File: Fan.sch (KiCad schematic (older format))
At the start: 9 parts, among them Q2 MOSFET_N, Q3 MOSFET_N, Q4 MOSFET_N, U4 OPA4170, U6 MCP4922-E/P

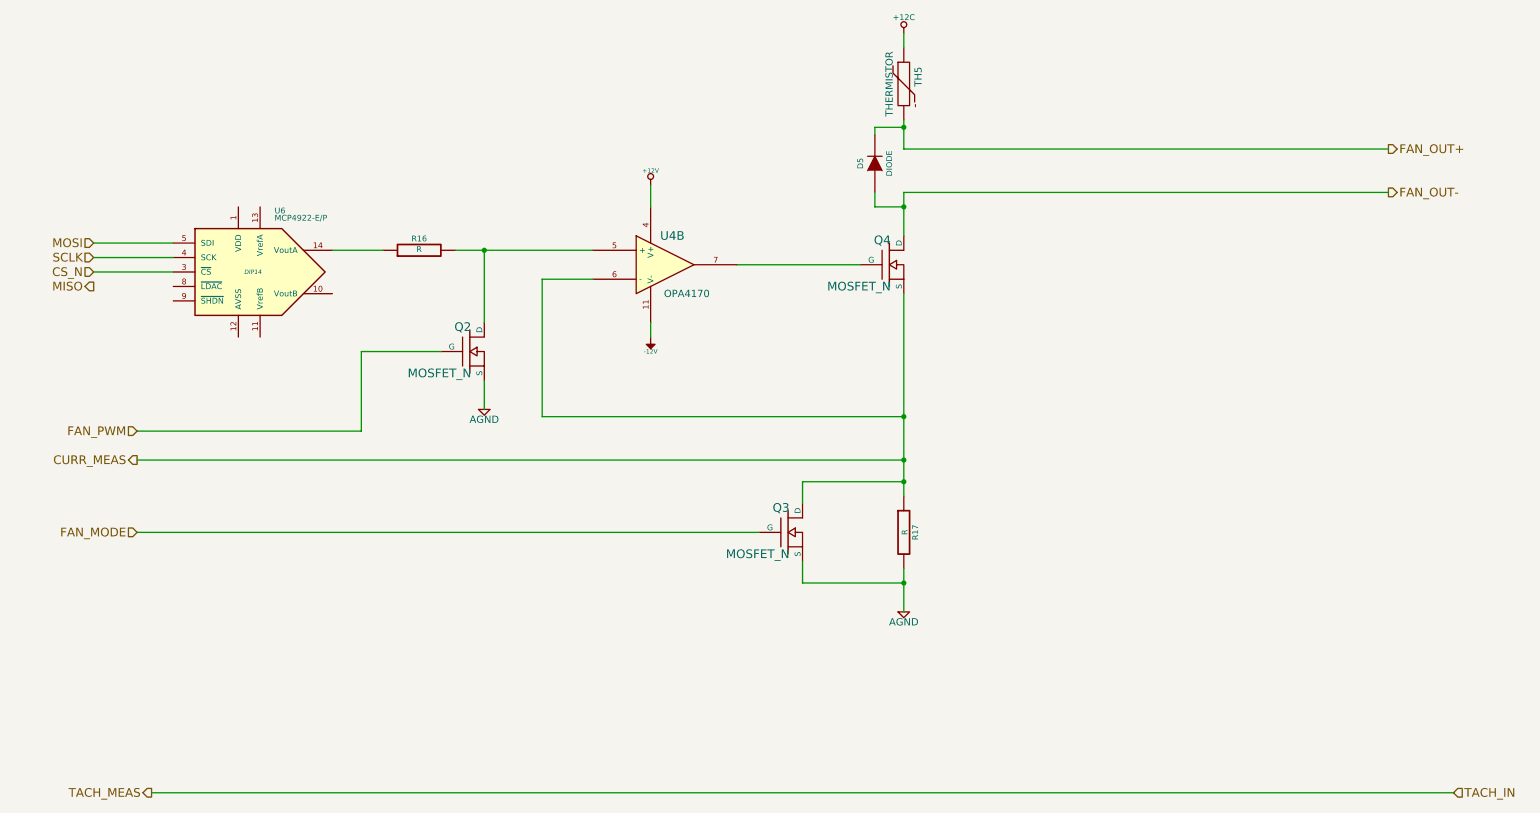
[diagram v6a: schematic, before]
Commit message: Fan driver: assc/placement
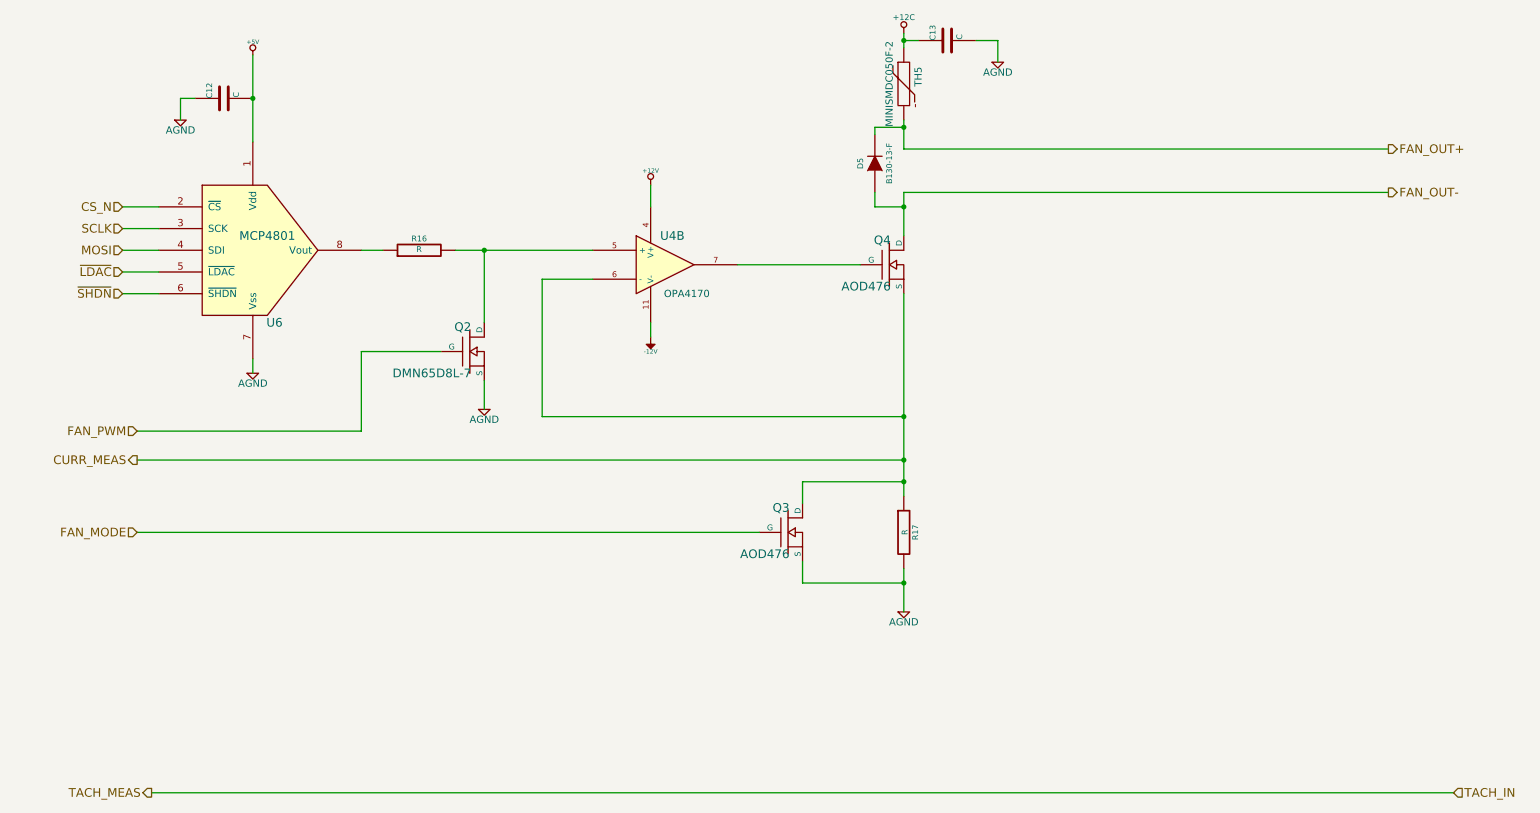
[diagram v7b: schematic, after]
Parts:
- removed Q3, Q4: MOSFET_N, ~, symbol MOSFET_N
- removed U6: MCP4922-E/P, DIP14, symbol MCP4922-E/P
- added C12, C13: C, ~, symbol C
- added Q3, Q4: AOD476, ~, symbol MOS_N_NUM
- added U6: MCP4801, symbol MCP4801
- D5: value DIODE -> B130-13-F; MFG Name (none) -> Diodes Inc; MFG Part Number (none) -> B130-13-F
- Q2: value MOSFET_N -> DMN65D8L-7; MFG Name (none) -> Diodes Inc; MFG Part Number (none) -> DMN65D8L-7
- TH5: value THERMISTOR -> MINISMDC050F-2; MFG Name (none) -> TE Connectivity; MFG Part Number (none) -> MINISMDC050F-2
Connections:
- net +12C: now also C13.1
- net AGND: now also C12.1, C13.2, Q3.3 (S), U6.7 (Vss)
- net CS_N: now also U6.2 (~CS)
- net CURR_MEAS: now also Q3.2 (D), Q4.3 (S)
- net FAN_MODE: now also Q3.1 (G)
- net FAN_OUT-: now also Q4.2 (D)
- net MOSI: now also U6.4 (SDI)
- net SCLK: now also U6.3 (SCK)
- net at U4.7: now also Q4.1 (G)
- net at R16.1: now also U6.8 (Vout)
- new net +5V: C12.2, U6.1 (Vdd)
- new net ~LDAC: U6.5 (~LDAC)
- new net ~SHDN: U6.6 (~SHDN)
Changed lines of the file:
@@
 $Descr A4 11693 8268
 encoding utf-8
-Sheet 5 9
+Sheet 4 9
 Title ""
-Date "22 feb 2014"
+Date "23 feb 2014"
 Rev ""
 Comp ""
@@
 $EndComp
 $Comp
-L MOSFET_N Q4
-U 1 1 52F44471
-P 6500 2500
-F 0 "Q4" H 6510 2670 60  0000 R CNN
-F 1 "MOSFET_N" H 6510 2350 60  0000 R CNN
-F 2 "~" H 6500 2500 60  0000 C CNN
-F 3 "~" H 6500 2500 60  0000 C CNN
-	1    6500 2500
-	1    0    0    -1
-$EndComp
-$Comp
 L R R17
 U 1 1 52F444AC
@@
 $EndComp
 $Comp
-L AGND #PWR25
+L AGND #PWR019
 U 1 1 52F444C1
 P 6600 4900
-F 0 "#PWR25" H 6600 4900 40  0001 C CNN
+F 0 "#PWR019" H 6600 4900 40  0001 C CNN
 F 1 "AGND" H 6600 4830 50  0000 C CNN
 F 2 "" H 6600 4900 60  0000 C CNN
@@
 $EndComp
 $Comp
-L +12V #PWR22
+L +12V #PWR020
 U 1 1 52F444E6
 P 4850 1950
-F 0 "#PWR22" H 4850 1900 20  0001 C CNN
+F 0 "#PWR020" H 4850 1900 20  0001 C CNN
 F 1 "+12V" H 4850 2050 30  0000 C CNN
 F 2 "" H 4850 1950 60  0000 C CNN
@@
 $EndComp
 $Comp
-L -12V #PWR23
+L -12V #PWR021
 U 1 1 52F444F9
 P 4850 3000
-F 0 "#PWR23" H 4850 3130 20  0001 C CNN
+F 0 "#PWR021" H 4850 3130 20  0001 C CNN
 F 1 "-12V" H 4850 3100 30  0000 C CNN
 F 2 "" H 4850 3000 60  0000 C CNN
@@
 $EndComp
 $Comp
-L AGND #PWR21
+L AGND #PWR022
 U 1 1 52F44588
 P 3700 3500
-F 0 "#PWR21" H 3700 3500 40  0001 C CNN
+F 0 "#PWR022" H 3700 3500 40  0001 C CNN
 F 1 "AGND" H 3700 3430 50  0000 C CNN
 F 2 "" H 3700 3500 60  0000 C CNN
@@
 	1    0    0    -1
 $EndComp
-$Comp
-L MCP4922-E/P U6
-U 1 1 52F445A1
-P 2100 2550
-F 0 "U6" H 2250 2950 40  0000 L BNN
-F 1 "MCP4922-E/P" H 2250 2900 40  0000 L BNN
-F 2 "DIP14" H 2100 2550 30  0000 C CIN
-F 3 "" H 2100 2550 60  0000 C CNN
-	1    2100 2550
-	1    0    0    -1
-$EndComp
 Text HLabel 1300 3850 0    60   Output ~ 0
 CURR_MEAS
-Text HLabel 1000 2350 0    60   Input ~ 0
+Text HLabel 1200 2400 0    60   Input ~ 0
 MOSI
-Text HLabel 1000 2650 0    60   Output ~ 0
-MISO
-Text HLabel 1000 2550 0    60   Input ~ 0
+Text HLabel 1200 2100 0    60   Input ~ 0
 CS_N
-Text HLabel 1000 2450 0    60   Input ~ 0
+Text HLabel 1200 2250 0    60   Input ~ 0
 SCLK
 Wire Wire Line
@@
 	1300 3850 6600 3850
 Connection ~ 6600 3850
-Wire Wire Line
-	1000 2350 1550 2350
-Wire Wire Line
-	1000 2450 1550 2450
-Wire Wire Line
-	1000 2550 1550 2550
 $Comp
 L R R16
@@
 	0    -1   -1   0
 $EndComp
-Wire Wire Line
-	3000 2400 2650 2400
-$Comp
-L MOSFET_N Q3
-U 1 1 52F7C941
-P 5800 4350
-F 0 "Q3" H 5810 4520 60  0000 R CNN
-F 1 "MOSFET_N" H 5810 4200 60  0000 R CNN
-F 2 "~" H 5800 4350 60  0000 C CNN
-F 3 "~" H 5800 4350 60  0000 C CNN
-	1    5800 4350
-	1    0    0    -1
-$EndComp
 $Comp
 L THERMISTOR TH5
@@
 P 6600 1250
 F 0 "TH5" V 6700 1300 50  0000 C CNN
-F 1 "THERMISTOR" V 6500 1250 50  0000 C CNN
+F 1 "MINISMDC050F-2" V 6500 1250 50  0000 C CNN
 F 2 "~" H 6600 1250 60  0000 C CNN
 F 3 "~" H 6600 1250 60  0000 C CNN
+F 4 "TE Connectivity" H 6600 1250 60  0001 C CNN "MFG Name"
+F 5 "MINISMDC050F-2" H 6600 1250 60  0001 C CNN "MFG Part Number"
 	1    6600 1250
 	1    0    0    -1
@@
 P 6400 1800
 F 0 "D5" H 6400 1900 40  0000 C CNN
-F 1 "DIODE" H 6400 1700 40  0000 C CNN
+F 1 "B130-13-F" H 6400 1700 40  0000 C CNN
 F 2 "~" H 6400 1800 60  0000 C CNN
 F 3 "~" H 6400 1800 60  0000 C CNN
+F 4 "Diodes Inc" H 6400 1800 60  0001 C CNN "MFG Name"
+F 5 "B130-13-F" H 6400 1800 60  0001 C CNN "MFG Part Number"
 	1    6400 1800
 	0    -1   -1   0
@@
 P 3600 3100
 F 0 "Q2" H 3610 3270 60  0000 R CNN
-F 1 "MOSFET_N" H 3610 2950 60  0000 R CNN
+F 1 "DMN65D8L-7" H 3610 2950 60  0000 R CNN
 F 2 "~" H 3600 3100 60  0000 C CNN
 F 3 "~" H 3600 3100 60  0000 C CNN
+F 4 "Diodes Inc" H 3600 3100 60  0001 C CNN "MFG Name"
+F 5 "DMN65D8L-7" H 3600 3100 60  0001 C CNN "MFG Part Number"
 	1    3600 3100
 	1    0    0    -1
@@
 FAN_MODE
 $Comp
-L +12C #PWR24
+L +12C #PWR023
 U 1 1 52F7D01B
 P 6600 900
-F 0 "#PWR24" H 6600 870 30  0001 C CNN
+F 0 "#PWR023" H 6600 870 30  0001 C CNN
 F 1 "+12C" H 6600 1010 40  0000 C CNN
 F 2 "" H 6600 900 60  0000 C CNN
@@
 	1    0    0    -1
 $EndComp
+$Comp
+L MCP4801 U6
+U 1 1 5309565C
+P 2100 2400
+F 0 "U6" H 2250 1900 60  0000 C CNN
+F 1 "MCP4801" H 2200 2500 60  0000 C CNN
+F 2 "" H 2200 2300 60  0000 C CNN
+F 3 "" H 2200 2300 60  0000 C CNN
+	1    2100 2400
+	1    0    0    -1
+$EndComp
+Wire Wire Line
+	2850 2400 3000 2400
+Wire Wire Line
+	1200 2100 1450 2100
+Wire Wire Line
+	1200 2250 1450 2250
+Wire Wire Line
+	1200 2400 1450 2400
+Text HLabel 1200 2550 0    60   Input ~ 0
+~LDAC
+Text HLabel 1200 2700 0    60   Input ~ 0
+~SHDN
+Wire Wire Line
+	1200 2550 1450 2550
+Wire Wire Line
+	1450 2700 1200 2700
+$Comp
+L +5V #PWR024
+U 1 1 5309ABB8
+P 2100 1050
+F 0 "#PWR024" H 2100 1140 20  0001 C CNN
+F 1 "+5V" H 2100 1140 30  0000 C CNN
+F 2 "" H 2100 1050 60  0000 C CNN
+F 3 "" H 2100 1050 60  0000 C CNN
+	1    2100 1050
+	1    0    0    -1
+$EndComp
+$Comp
+L C C12
+U 1 1 5309ABC7
+P 1900 1350
+F 0 "C12" H 1900 1450 40  0000 L CNN
+F 1 "C" H 1906 1265 40  0000 L CNN
+F 2 "~" H 1938 1200 30  0000 C CNN
+F 3 "~" H 1900 1350 60  0000 C CNN
+	1    1900 1350
+	0    -1   -1   0
+$EndComp
+$Comp
+L AGND #PWR025
+U 1 1 5309ABE0
+P 1600 1500
+F 0 "#PWR025" H 1600 1500 40  0001 C CNN
+F 1 "AGND" H 1600 1430 50  0000 C CNN
+F 2 "" H 1600 1500 60  0000 C CNN
+F 3 "" H 1600 1500 60  0000 C CNN
+	1    1600 1500
+	1    0    0    -1
+$EndComp
+Wire Wire Line
+	1600 1500 1600 1350
+Wire Wire Line
+	1600 1350 1700 1350
+Wire Wire Line
+	2100 1050 2100 1650
+Connection ~ 2100 1350
+$Comp
+L AGND #PWR026
+U 1 1 5309ACA6
+P 2100 3250
+F 0 "#PWR026" H 2100 3250 40  0001 C CNN
+F 1 "AGND" H 2100 3180 50  0000 C CNN
+F 2 "" H 2100 3250 60  0000 C CNN
+F 3 "" H 2100 3250 60  0000 C CNN
+	1    2100 3250
+	1    0    0    -1
+$EndComp
+Wire Wire Line
+	2100 3250 2100 3150
+$Comp
+L C C13
+U 1 1 5309B996
+P 6900 950
+F 0 "C13" H 6900 1050 40  0000 L CNN
+F 1 "C" H 6906 865 40  0000 L CNN
+F 2 "~" H 6938 800 30  0000 C CNN
+F 3 "~" H 6900 950 60  0000 C CNN
+	1    6900 950
+	0    -1   -1   0
+$EndComp
+$Comp
+L AGND #PWR027
+U 1 1 5309B99C
+P 7250 1100
+F 0 "#PWR027" H 7250 1100 40  0001 C CNN
+F 1 "AGND" H 7250 1030 50  0000 C CNN
+F 2 "" H 7250 1100 60  0000 C CNN
+F 3 "" H 7250 1100 60  0000 C CNN
+	1    7250 1100
+	1    0    0    -1
+$EndComp
+Wire Wire Line
+	7100 950  7250 950
+Wire Wire Line
+	7250 950  7250 1100
+Wire Wire Line
+	6700 950  6600 950
+Connection ~ 6600 950
+$Comp
+L MOS_N_NUM Q4
+U 1 1 5309BD63
+P 6500 2500
+F 0 "Q4" H 6510 2670 60  0000 R CNN
+F 1 "AOD476" H 6510 2350 60  0000 R CNN
+F 2 "~" H 6500 2500 60  0000 C CNN
+F 3 "~" H 6500 2500 60  0000 C CNN
+F 4 "Alpha and Omega" H 6500 2500 60  0001 C CNN "MFG Name"
+F 5 "AOD476" H 6500 2500 60  0001 C CNN "MFG Part Number"
+	1    6500 2500
+	1    0    0    -1
+$EndComp
+$Comp
+L MOS_N_NUM Q3
+U 1 1 5309BDCE
+P 5800 4350
+F 0 "Q3" H 5810 4520 60  0000 R CNN
+F 1 "AOD476" H 5810 4200 60  0000 R CNN
+F 2 "~" H 5800 4350 60  0000 C CNN
+F 3 "~" H 5800 4350 60  0000 C CNN
+F 4 "Alpha and Omega" H 5800 4350 60  0001 C CNN "MFG Name"
+F 5 "AOD476" H 5800 4350 60  0001 C CNN "MFG Part Number"
+	1    5800 4350
+	1    0    0    -1
+$EndComp
